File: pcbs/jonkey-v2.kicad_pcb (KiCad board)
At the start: 2 copper layers, 191.4 x 129.7 mm, 156 parts

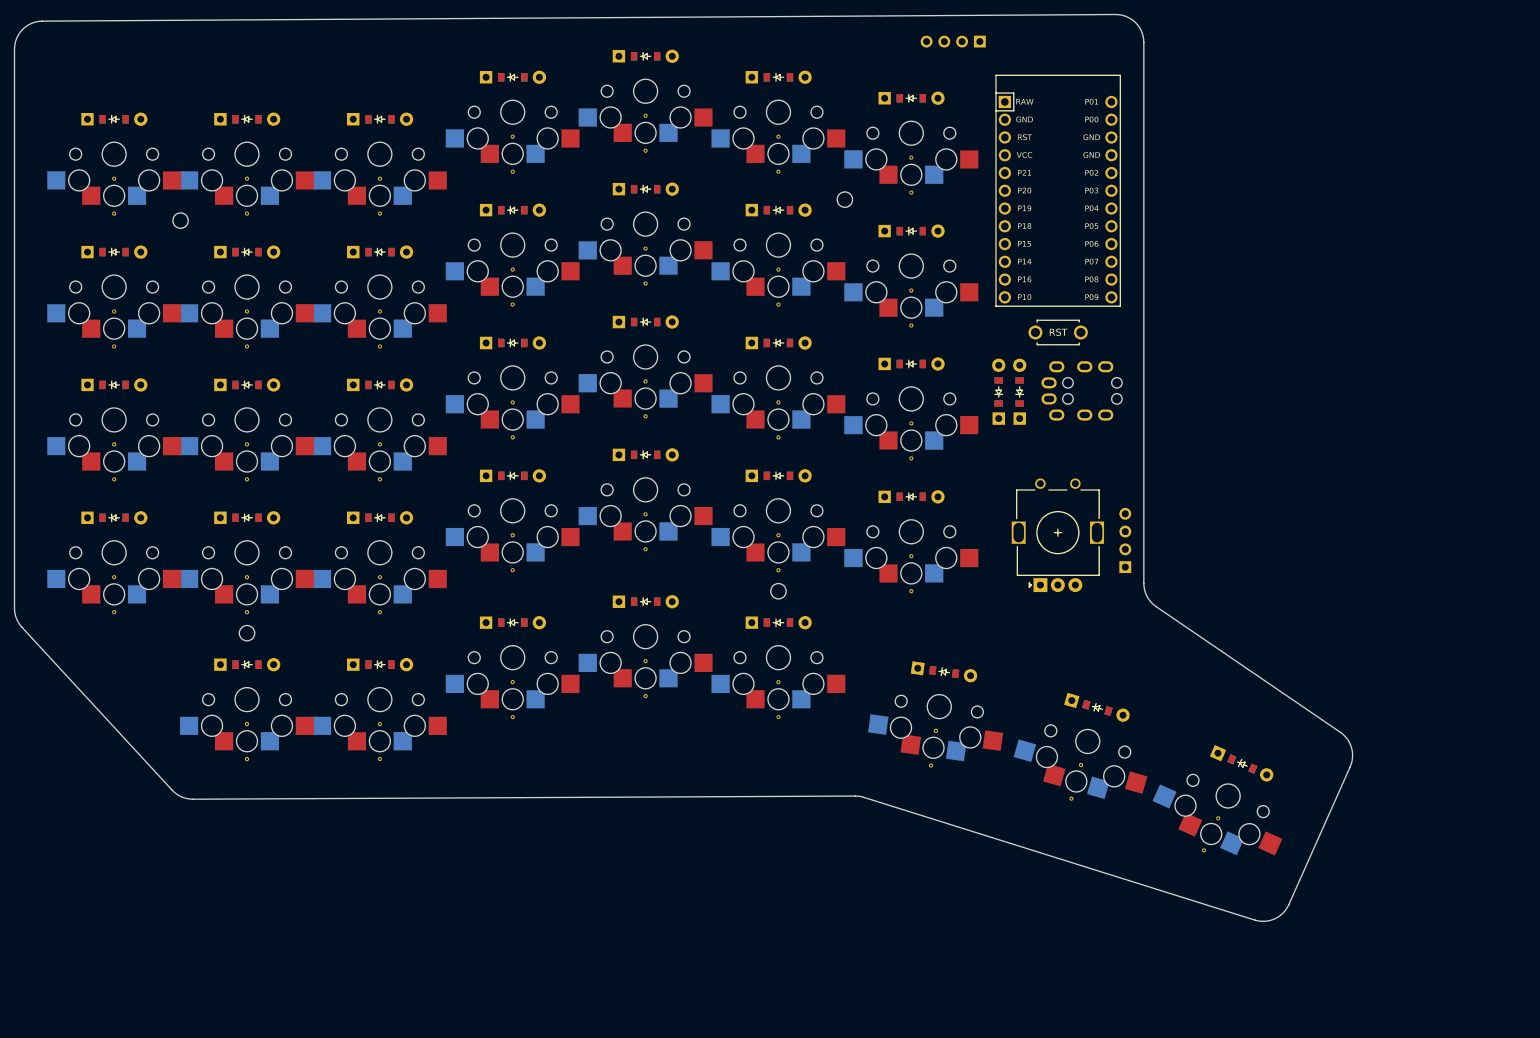
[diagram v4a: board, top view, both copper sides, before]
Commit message: feat: routing done + switch P2 and P3 resistor placement for easier routing
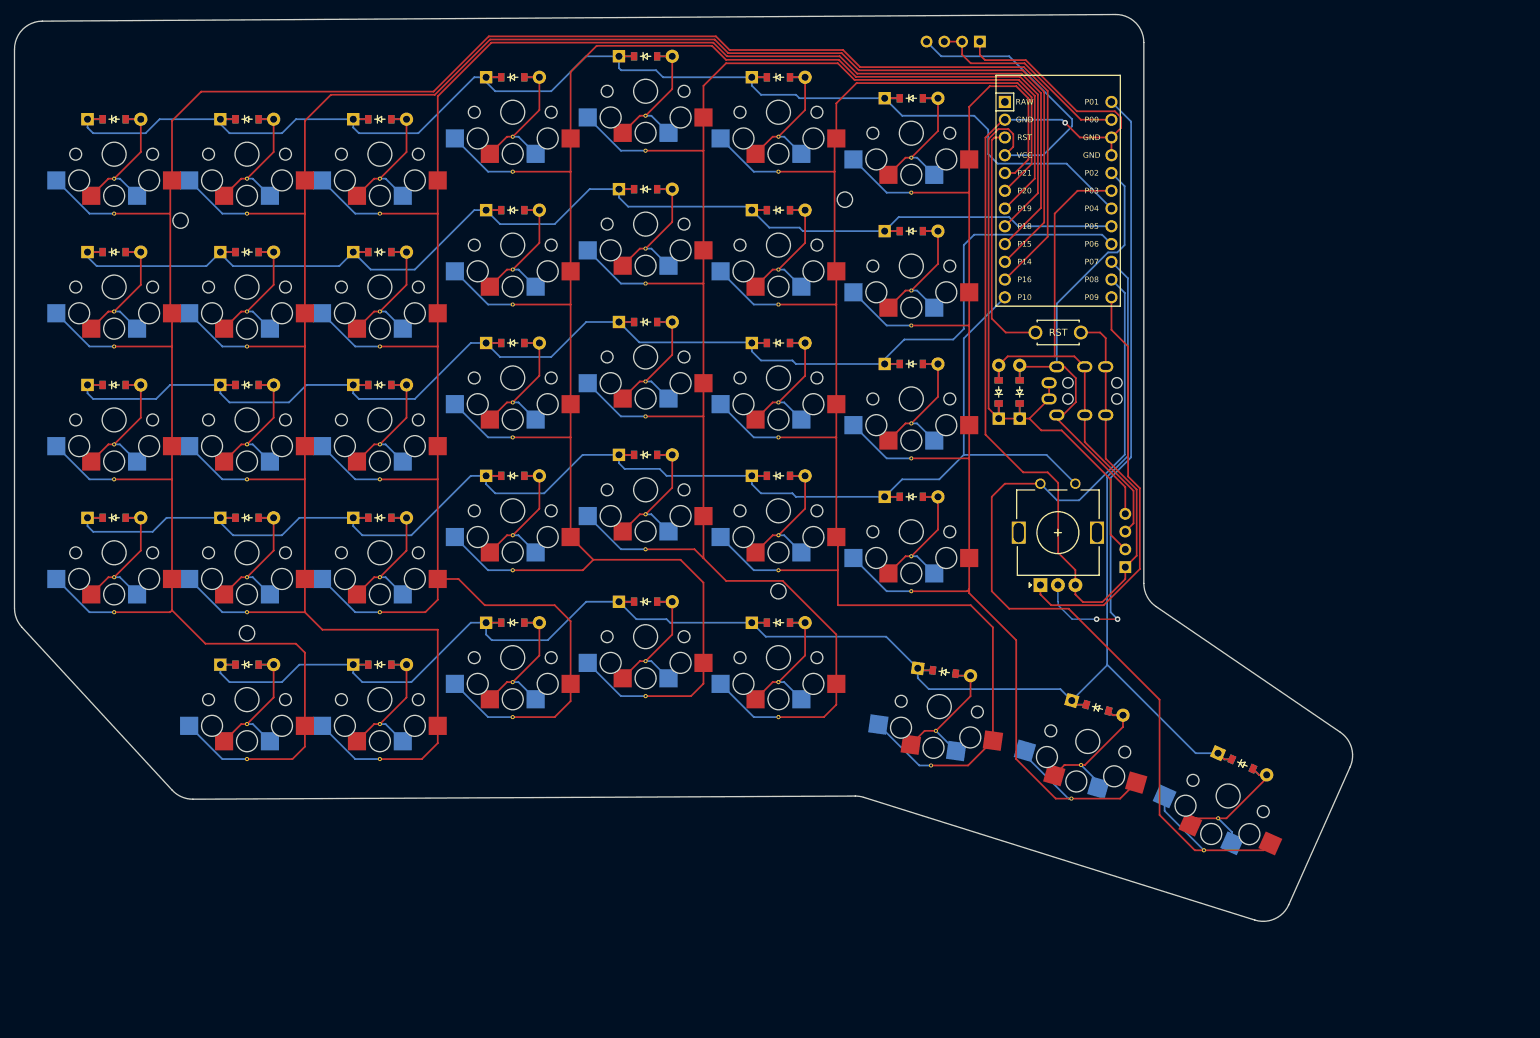
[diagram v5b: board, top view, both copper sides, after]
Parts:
- SERIAL1: value OLED -> SERIAL
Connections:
- R11 pad 2: P2 -> P3
- R21 pad 2: P3 -> P2
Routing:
- net P16: track 0.00 -> 361.3 mm
- net P14: track 0.00 -> 340.3 mm
- net P15: track 0.00 -> 315.4 mm
- net P18: track 0.00 -> 291.9 mm
- net P7: track 0.00 -> 264.3 mm
- net P19: track 0.00 -> 263.5 mm
- net P20: track 0.00 -> 251.0 mm
- net P21: track 0.00 -> 223.9 mm
- net P10: track 0.00 -> 218.6 mm
- net P6: track 0.00 -> 208.5 mm
- net P4: track 0.00 -> 202.0 mm
- net P5: track 0.00 -> 192.5 mm
- net GND: track 0.00 -> 174.4 mm, vias 0 -> 1
- net P8: track 0.00 -> 138.1 mm
- net VCC: track 0.00 -> 131.7 mm
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
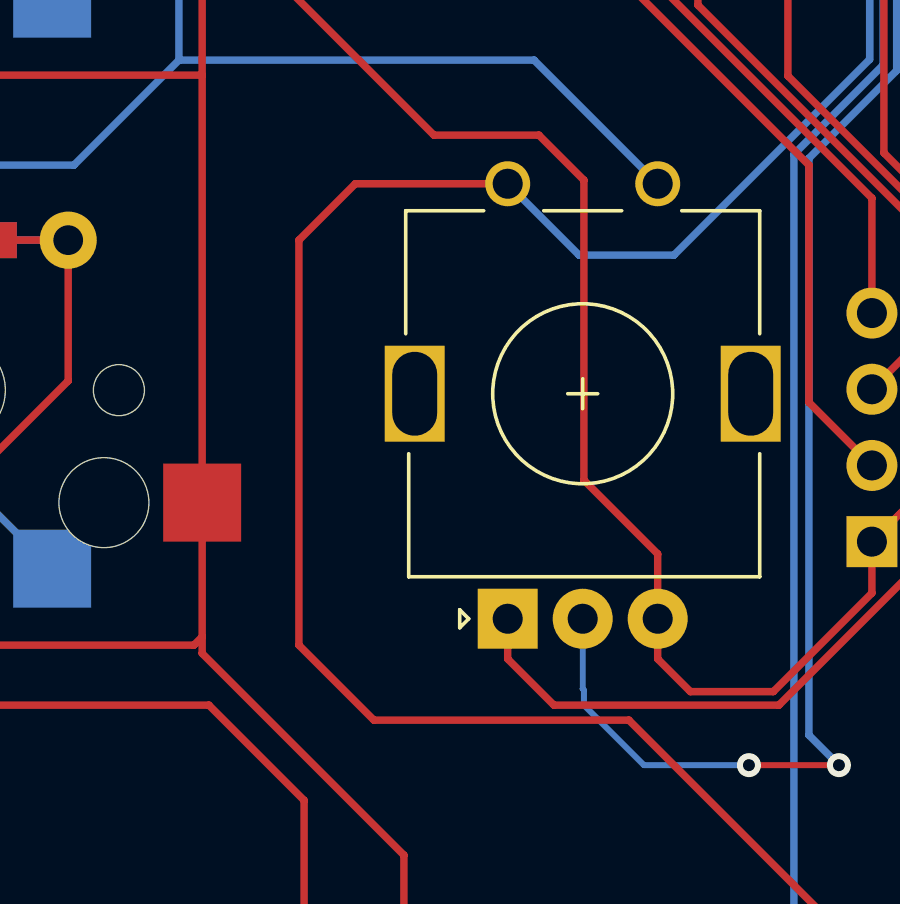
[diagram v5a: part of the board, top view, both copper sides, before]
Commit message: feat: check in latest PCBs (wrong pins for encoder)
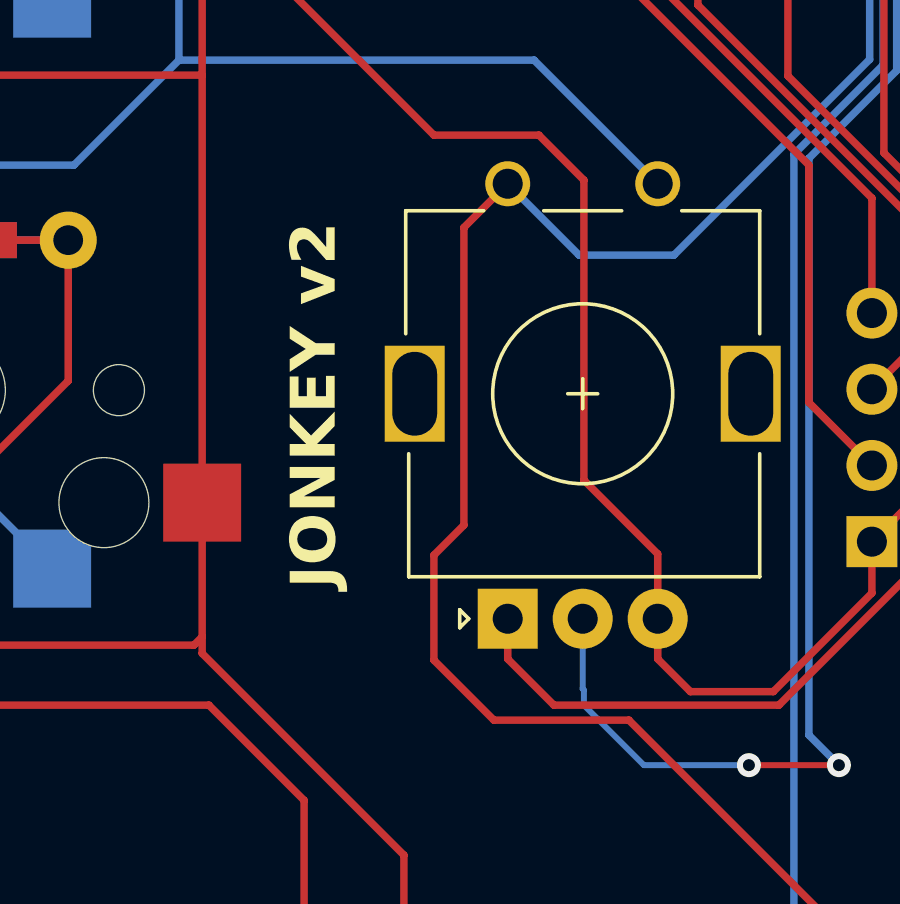
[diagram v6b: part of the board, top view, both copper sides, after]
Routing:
- net P8: track 138.1 -> 129.1 mm
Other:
- board text added: "JONKEY v2"
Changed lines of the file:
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@@
 			(outputformat 1)
 			(mirror no)
-			(drillshape 1)
+			(drillshape 0)
 			(scaleselection 1)
 			(outputdirectory "")
@@
 		(layer "Edge.Cuts")
 	)
+	(gr_text "JONKEY v2"
+		(at 233.5 151 90)
+		(layer "B.SilkS")
+		(effects
+			(font
+				(size 1.5 1.5)
+				(thickness 0.3)
+				(bold yes)
+			)
+			(justify mirror)
+		)
+	)
+	(gr_text "JONKEY v2"
+		(at 233.5 151 90)
+		(layer "F.SilkS")
+		(effects
+			(font
+				(size 1.5 1.5)
+				(thickness 0.3)
+				(bold yes)
+			)
+		)
+	)
 	(segment
 		(start 111.31 148.5)
@@
 	)
 	(segment
-		(start 235.5 161.5)
-		(end 233 159)
+		(start 239.5 161.5)
+		(end 237.5 159.5)
+		(width 0.25)
+		(layer "F.Cu")
+		(net 49)
+	)
+	(segment
+		(start 238.5 145.08)
+		(end 239.96 143.62)
 		(width 0.25)
 		(layer "F.Cu")
@@
 	(segment
 		(start 244 161.5)
-		(end 235.5 161.5)
+		(end 239.5 161.5)
 		(width 0.25)
 		(layer "F.Cu")
@@
 	)
 	(segment
-		(start 262.045148 196.045148)
-		(end 257 191)
+		(start 237.5 159.5)
+		(end 237.5 156)
 		(width 0.25)
 		(layer "F.Cu")
@@
 	)
 	(segment
-		(start 233 159)
-		(end 233 145.5)
+		(start 257 191)
+		(end 257 174.5)
 		(width 0.25)
 		(layer "F.Cu")
@@
 	)
 	(segment
-		(start 233 145.5)
-		(end 234.88 143.62)
+		(start 257 174.5)
+		(end 244 161.5)
 		(width 0.25)
 		(layer "F.Cu")
@@
 	)
 	(segment
-		(start 257 191)
-		(end 257 174.5)
+		(start 238.5 155)
+		(end 238.5 145.08)
 		(width 0.25)
 		(layer "F.Cu")
@@
 	)
 	(segment
-		(start 272.841034 195.071553)
-		(end 271.867439 196.045148)
+		(start 263.349447 196.045148)
+		(end 262.045148 196.045148)
 		(width 0.25)
 		(layer "F.Cu")
@@
 	)
 	(segment
-		(start 234.88 143.62)
-		(end 239.96 143.62)
+		(start 237.5 156)
+		(end 238.5 155)
 		(width 0.25)
 		(layer "F.Cu")
@@
 	)
 	(segment
-		(start 263.349447 196.045148)
-		(end 262.045148 196.045148)
+		(start 262.045148 196.045148)
+		(end 257 191)
 		(width 0.25)
 		(layer "F.Cu")
@@
 	)
 	(segment
-		(start 257 174.5)
-		(end 244 161.5)
+		(start 272.841034 195.071553)
+		(end 271.867439 196.045148)
 		(width 0.25)
 		(layer "F.Cu")
